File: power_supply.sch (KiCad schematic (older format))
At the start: 95 parts, among them J1 USB-IN, J2 USB OUT, Q1 SI4174DY, Q2 SI4463CDY, Q3 SI4463CDY, U1 LM3914, U10 FDC6392S, U11 MCP6041, U2 TPD2E001, U3 MIC2185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

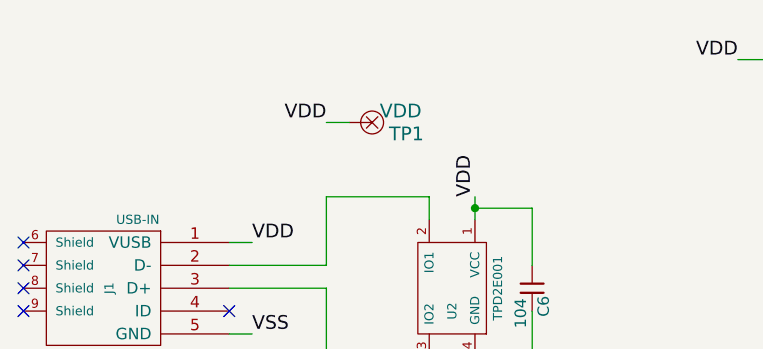
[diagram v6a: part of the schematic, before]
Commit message: Added test points
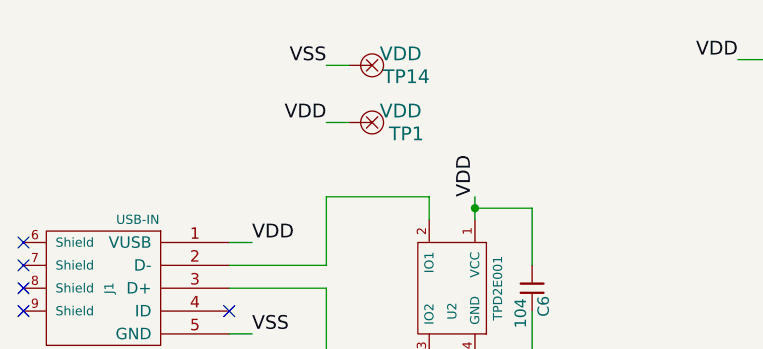
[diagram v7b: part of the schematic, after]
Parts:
- added TP14: VDD, TP, symbol TP
- TP1, TP10, TP11, TP12, TP13, TP2, TP3, TP4, TP6, TP7, TP8, TP9: footprint (none) -> TP; Product Number (none) -> 5000K-ND; Vendor (none) -> Digikey
- TP5: footprint (none) -> TP
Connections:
- net VSS: now also TP14.1
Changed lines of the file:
@@
 F 0 "TP1" H 2450 1050 60  0000 C CNN
 F 1 "VDD" H 2425 1150 60  0000 C CNN
-F 2 "" H 2300 1100 60  0000 C CNN
-F 3 "" H 2300 1100 60  0000 C CNN
+F 2 "TP" H 2300 1100 60  0001 C CNN
+F 3 "http://www.keyelco.com/userAssets/file/M60-2p60.pdf" H 2300 1100 60  0001 C CNN
+F 4 "5000K-ND" H 2300 1100 60  0001 C CNN "Product Number"
+F 5 "Digikey" H 2300 1100 60  0001 C CNN "Vendor"
 	1    2300 1100
 	1    0    0    -1
@@
 Text Label 2100 1100 2    60   ~ 0
 VDD
-$Comp
-L TP TP6
-U 1 1 53A9ABF0
-P 7600 1950
-F 0 "TP6" H 7750 1900 60  0000 C CNN
-F 1 "VBAT" H 7725 2000 60  0000 C CNN
-F 2 "" H 7600 1950 60  0000 C CNN
-F 3 "" H 7600 1950 60  0000 C CNN
-	1    7600 1950
-	1    0    0    -1
-$EndComp
 Wire Wire Line
 	4500 1975 4500 1625
@@
 	7500 1950 7375 1950
 Connection ~ 7375 1950
-$Comp
-L TP TP11
-U 1 1 53A9AEB5
-P 10200 1575
-F 0 "TP11" H 10350 1525 60  0000 C CNN
-F 1 "VSYS" H 10325 1625 60  0000 C CNN
-F 2 "" H 10200 1575 60  0000 C CNN
-F 3 "" H 10200 1575 60  0000 C CNN
-	1    10200 1575
-	1    0    0    -1
-$EndComp
 Wire Wire Line
 	10100 1575 9975 1575
 Connection ~ 9975 1575
-$Comp
-L TP TP10
-U 1 1 53A9B01C
-P 9800 3075
-F 0 "TP10" H 9950 3025 60  0000 C CNN
-F 1 "RS+" H 9925 3125 60  0000 C CNN
-F 2 "" H 9800 3075 60  0000 C CNN
-F 3 "" H 9800 3075 60  0000 C CNN
-	1    9800 3075
-	0    -1   -1   0
-$EndComp
 Wire Wire Line
 	9800 3175 9800 3250
 Connection ~ 9800 3250
-$Comp
-L TP TP9
-U 1 1 53A9B185
-P 9775 3875
-F 0 "TP9" H 9925 3825 60  0000 C CNN
-F 1 "RS-" H 9900 3925 60  0000 C CNN
-F 2 "" H 9775 3875 60  0000 C CNN
-F 3 "" H 9775 3875 60  0000 C CNN
-	1    9775 3875
-	0    1    1    0
-$EndComp
 Wire Wire Line
 	9775 3700 9775 3775
 Connection ~ 9775 3700
-$Comp
-L TP TP13
-U 1 1 53A9B5CD
-P 10625 4025
-F 0 "TP13" H 10775 3975 60  0000 C CNN
-F 1 "VDISP" H 10750 4075 60  0000 C CNN
-F 2 "" H 10625 4025 60  0000 C CNN
-F 3 "" H 10625 4025 60  0000 C CNN
-	1    10625 4025
-	0    -1   -1   0
-$EndComp
 Wire Wire Line
 	10625 4125 10625 4250
 Connection ~ 10625 4250
-$Comp
-L TP TP8
-U 1 1 53A9B73A
-P 9000 3850
-F 0 "TP8" H 9150 3800 60  0000 C CNN
-F 1 "VSENSE" H 9125 3900 60  0000 C CNN
-F 2 "" H 9000 3850 60  0000 C CNN
-F 3 "" H 9000 3850 60  0000 C CNN
-	1    9000 3850
-	0    1    1    0
-$EndComp
 Wire Wire Line
 	9000 3750 9000 3575
 Connection ~ 9000 3575
-$Comp
-L TP TP12
-U 1 1 53A9B8B3
-P 10375 4975
-F 0 "TP12" H 10525 4925 60  0000 C CNN
-F 1 "VSW_OUT" H 10500 5025 60  0000 C CNN
-F 2 "" H 10375 4975 60  0000 C CNN
-F 3 "" H 10375 4975 60  0000 C CNN
-	1    10375 4975
-	0    1    1    0
-$EndComp
 Connection ~ 10375 4800
-$Comp
-L TP TP2
-U 1 1 53A9BA2E
-P 4875 6650
-F 0 "TP2" H 5025 6600 60  0000 C CNN
-F 1 "VUSB" H 5000 6700 60  0000 C CNN
-F 2 "" H 4875 6650 60  0000 C CNN
-F 3 "" H 4875 6650 60  0000 C CNN
-	1    4875 6650
-	-1   0    0    1
-$EndComp
 Wire Wire Line
 	4975 6650 5075 6650
 Connection ~ 5075 6650
-$Comp
-L TP TP3
-U 1 1 53A9BBA0
-P 5900 6800
-F 0 "TP3" H 6050 6750 60  0000 C CNN
-F 1 "D-" H 6025 6850 60  0000 C CNN
-F 2 "" H 5900 6800 60  0000 C CNN
-F 3 "" H 5900 6800 60  0000 C CNN
-	1    5900 6800
-	0    1    1    0
-$EndComp
 Wire Wire Line
 	5900 6700 5900 6625
 Connection ~ 5900 6625
-$Comp
-L TP TP4
-U 1 1 53A9BD14
-P 6625 6775
-F 0 "TP4" H 6775 6725 60  0000 C CNN
-F 1 "D+" H 6750 6825 60  0000 C CNN
-F 2 "" H 6625 6775 60  0000 C CNN
-F 3 "" H 6625 6775 60  0000 C CNN
-	1    6625 6775
-	0    1    1    0
-$EndComp
 Wire Wire Line
 	6625 6675 6625 6625
 Connection ~ 6625 6625
-$Comp
-L TP TP7
-U 1 1 53A9C03D
-P 7725 4975
-F 0 "TP7" H 7875 4925 60  0000 C CNN
-F 1 "VSW_REF" H 7850 5025 60  0000 C CNN
-F 2 "" H 7725 4975 60  0000 C CNN
-F 3 "" H 7725 4975 60  0000 C CNN
-	1    7725 4975
-	-1   0    0    1
-$EndComp
 Connection ~ 7950 4975
 $Comp
@@
 F 0 "TP5" H 6975 3400 60  0000 C CNN
 F 1 "VREG" H 6950 3500 60  0000 C CNN
-F 2 "" H 6825 3450 60  0000 C CNN
+F 2 "TP" H 6825 3450 60  0001 C CNN
 F 3 "" H 6825 3450 60  0000 C CNN
 	1    6825 3450
@@
 Connection ~ 9350 850
 Connection ~ 9500 850
+Wire Wire Line
+	2200 850  2100 850
+Text Label 2100 850  2    60   ~ 0
+VSS
+$Comp
+L TP TP2
+U 1 1 53A9D1FA
+P 4875 6650
+F 0 "TP2" H 5025 6600 60  0000 C CNN
+F 1 "VUSB" H 5000 6700 60  0000 C CNN
+F 2 "TP" H 4875 6650 60  0001 C CNN
+F 3 "http://www.keyelco.com/userAssets/file/M60-2p60.pdf" H 4875 6650 60  0001 C CNN
+F 4 "5000K-ND" H 4875 6650 60  0001 C CNN "Product Number"
+F 5 "Digikey" H 4875 6650 60  0001 C CNN "Vendor"
+	1    4875 6650
+	-1   0    0    1
+$EndComp
+$Comp
+L TP TP3
+U 1 1 53A9D210
+P 5900 6800
+F 0 "TP3" H 6050 6750 60  0000 C CNN
+F 1 "D-" H 6025 6850 60  0000 C CNN
+F 2 "TP" H 5900 6800 60  0001 C CNN
+F 3 "http://www.keyelco.com/userAssets/file/M60-2p60.pdf" H 5900 6800 60  0001 C CNN
+F 4 "5000K-ND" H 5900 6800 60  0001 C CNN "Product Number"
+F 5 "Digikey" H 5900 6800 60  0001 C CNN "Vendor"
+	1    5900 6800
+	0    1    1    0
+$EndComp
+$Comp
+L TP TP4
+U 1 1 53A9D226
+P 6625 6775
+F 0 "TP4" H 6775 6725 60  0000 C CNN
+F 1 "D+" H 6750 6825 60  0000 C CNN
+F 2 "TP" H 6625 6775 60  0001 C CNN
+F 3 "http://www.keyelco.com/userAssets/file/M60-2p60.pdf" H 6625 6775 60  0001 C CNN
+F 4 "5000K-ND" H 6625 6775 60  0001 C CNN "Product Number"
+F 5 "Digikey" H 6625 6775 60  0001 C CNN "Vendor"
+	1    6625 6775
+	0    1    1    0
+$EndComp
+$Comp
+L TP TP7
+U 1 1 53A9D23C
+P 7725 4975
+F 0 "TP7" H 7875 4925 60  0000 C CNN
+F 1 "VSW_REF" H 7850 5025 60  0000 C CNN
+F 2 "TP" H 7725 4975 60  0001 C CNN
+F 3 "http://www.keyelco.com/userAssets/file/M60-2p60.pdf" H 7725 4975 60  0001 C CNN
+F 4 "5000K-ND" H 7725 4975 60  0001 C CNN "Product Number"
+F 5 "Digikey" H 7725 4975 60  0001 C CNN "Vendor"
+	1    7725 4975
+	-1   0    0    1
+$EndComp
+$Comp
+L TP TP12
+U 1 1 53A9D252
+P 10375 4975
+F 0 "TP12" H 10525 4925 60  0000 C CNN
+F 1 "VSW_OUT" H 10500 5025 60  0000 C CNN
+F 2 "TP" H 10375 4975 60  0001 C CNN
+F 3 "http://www.keyelco.com/userAssets/file/M60-2p60.pdf" H 10375 4975 60  0001 C CNN
+F 4 "5000K-ND" H 10375 4975 60  0001 C CNN "Product Number"
+F 5 "Digikey" H 10375 4975 60  0001 C CNN "Vendor"
+	1    10375 4975
+	0    1    1    0
+$EndComp
+$Comp
+L TP TP13
+U 1 1 53A9D25A
+P 10625 4025
+F 0 "TP13" H 10775 3975 60  0000 C CNN
+F 1 "VDISP" H 10750 4075 60  0000 C CNN
+F 2 "TP" H 10625 4025 60  0001 C CNN
+F 3 "http://www.keyelco.com/userAssets/file/M60-2p60.pdf" H 10625 4025 60  0001 C CNN
+F 4 "5000K-ND" H 10625 4025 60  0001 C CNN "Product Number"
+F 5 "Digikey" H 10625 4025 60  0001 C CNN "Vendor"
+	1    10625 4025
+	0    -1   -1   0
+$EndComp
+$Comp
+L TP TP9
+U 1 1 53A9D270
+P 9775 3875
+F 0 "TP9" H 9925 3825 60  0000 C CNN
+F 1 "RS-" H 9900 3925 60  0000 C CNN
+F 2 "TP" H 9775 3875 60  0001 C CNN
+F 3 "http://www.keyelco.com/userAssets/file/M60-2p60.pdf" H 9775 3875 60  0001 C CNN
+F 4 "5000K-ND" H 9775 3875 60  0001 C CNN "Product Number"
+F 5 "Digikey" H 9775 3875 60  0001 C CNN "Vendor"
+	1    9775 3875
+	0    1    1    0
+$EndComp
+$Comp
+L TP TP8
+U 1 1 53A9D278
+P 9000 3850
+F 0 "TP8" H 9150 3800 60  0000 C CNN
+F 1 "VSENSE" H 9125 3900 60  0000 C CNN
+F 2 "TP" H 9000 3850 60  0001 C CNN
+F 3 "http://www.keyelco.com/userAssets/file/M60-2p60.pdf" H 9000 3850 60  0001 C CNN
+F 4 "5000K-ND" H 9000 3850 60  0001 C CNN "Product Number"
+F 5 "Digikey" H 9000 3850 60  0001 C CNN "Vendor"
+	1    9000 3850
+	0    1    1    0
+$EndComp
+$Comp
+L TP TP6
+U 1 1 53A9D28E
+P 7600 1950
+F 0 "TP6" H 7750 1900 60  0000 C CNN
+F 1 "VBAT" H 7725 2000 60  0000 C CNN
+F 2 "TP" H 7600 1950 60  0001 C CNN
+F 3 "http://www.keyelco.com/userAssets/file/M60-2p60.pdf" H 7600 1950 60  0001 C CNN
+F 4 "5000K-ND" H 7600 1950 60  0001 C CNN "Product Number"
+F 5 "Digikey" H 7600 1950 60  0001 C CNN "Vendor"
+	1    7600 1950
+	1    0    0    -1
+$EndComp
+$Comp
+L TP TP11
+U 1 1 53A9D2C0
+P 10200 1575
+F 0 "TP11" H 10350 1525 60  0000 C CNN
+F 1 "VSYS" H 10325 1625 60  0000 C CNN
+F 2 "TP" H 10200 1575 60  0001 C CNN
+F 3 "http://www.keyelco.com/userAssets/file/M60-2p60.pdf" H 10200 1575 60  0001 C CNN
+F 4 "5000K-ND" H 10200 1575 60  0001 C CNN "Product Number"
+F 5 "Digikey" H 10200 1575 60  0001 C CNN "Vendor"
+	1    10200 1575
+	1    0    0    -1
+$EndComp
+$Comp
+L TP TP10
+U 1 1 53A9D48F
+P 9800 3075
+F 0 "TP10" H 9950 3025 60  0000 C CNN
+F 1 "RS+" H 9925 3125 60  0000 C CNN
+F 2 "TP" H 9800 3075 60  0001 C CNN
+F 3 "http://www.keyelco.com/userAssets/file/M60-2p60.pdf" H 9800 3075 60  0001 C CNN
+F 4 "5000K-ND" H 9800 3075 60  0001 C CNN "Product Number"
+F 5 "Digikey" H 9800 3075 60  0001 C CNN "Vendor"
+	1    9800 3075
+	0    -1   -1   0
+$EndComp
+$Comp
+L TP TP14
+U 1 1 53A9D69D
+P 2300 850
+F 0 "TP14" H 2450 800 60  0000 C CNN
+F 1 "VDD" H 2425 900 60  0000 C CNN
+F 2 "TP" H 2300 850 60  0001 C CNN
+F 3 "http://www.keyelco.com/userAssets/file/M60-2p60.pdf" H 2300 850 60  0001 C CNN
+F 4 "5000K-ND" H 2300 850 60  0001 C CNN "Product Number"
+F 5 "Digikey" H 2300 850 60  0001 C CNN "Vendor"
+	1    2300 850
+	1    0    0    -1
+$EndComp
 $EndSCHEMATC

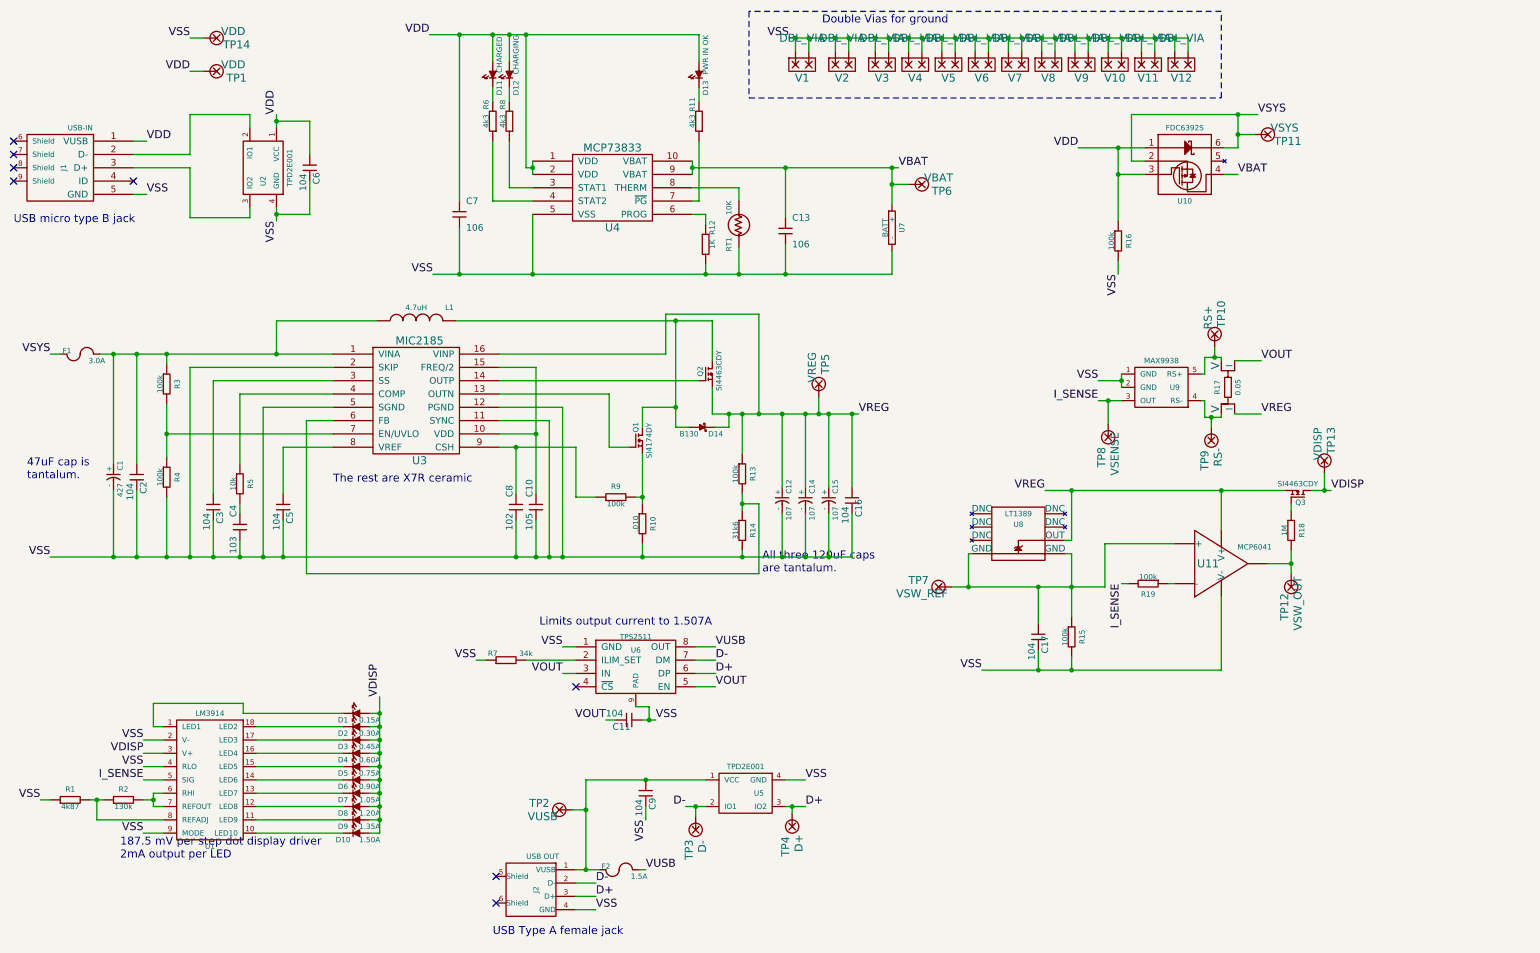
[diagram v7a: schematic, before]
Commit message: Added silkscreen
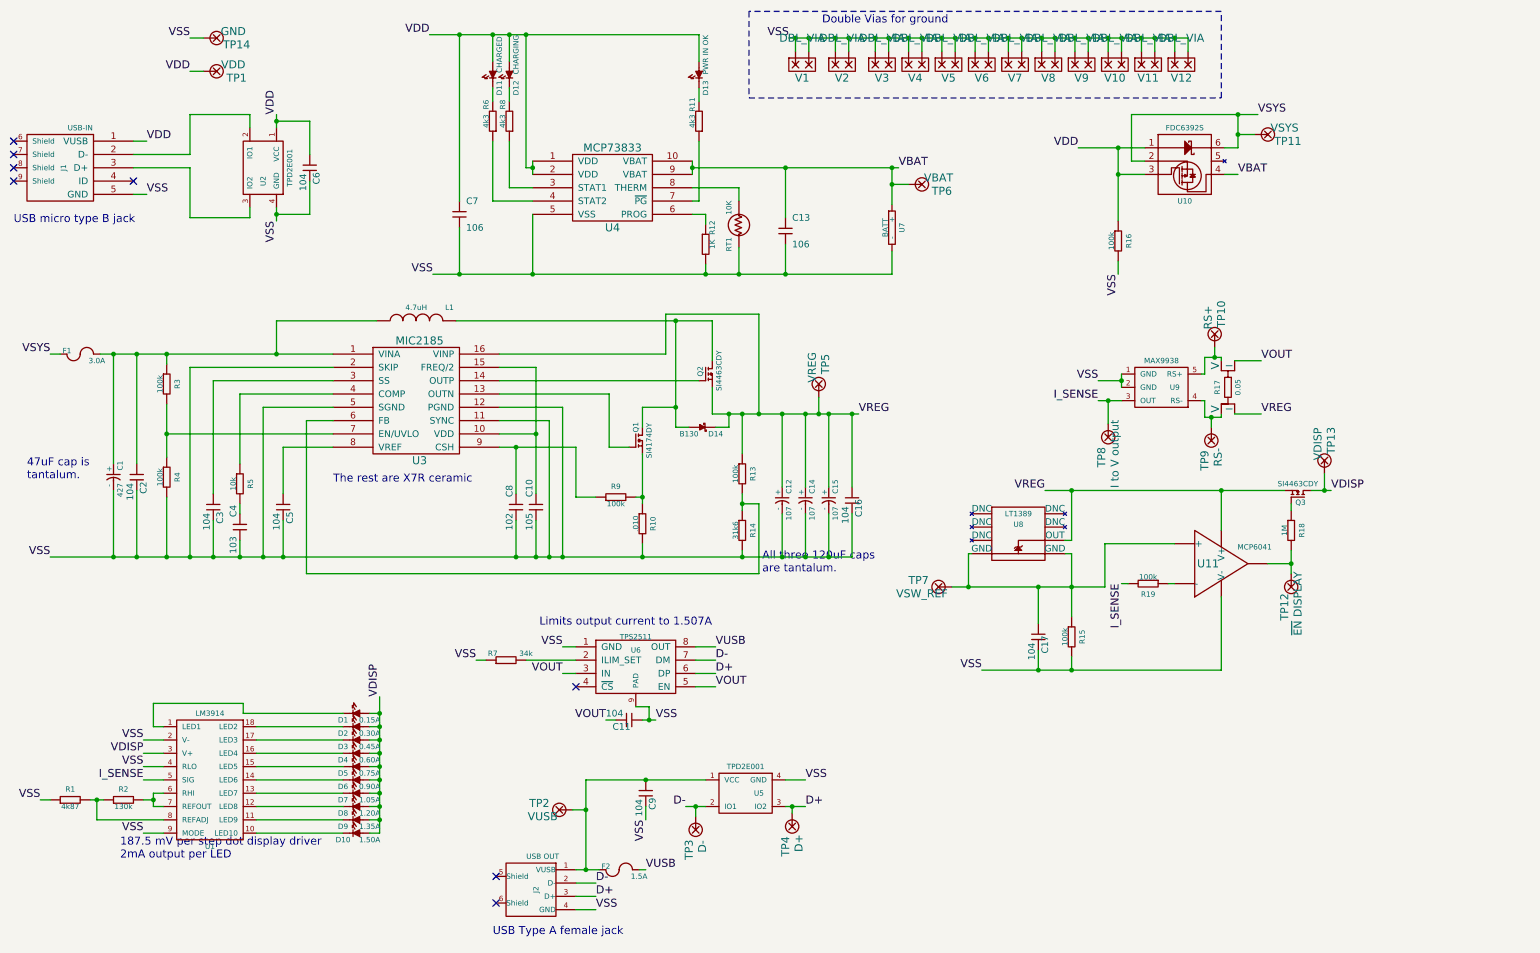
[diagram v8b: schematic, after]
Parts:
- TP12: value VSW_OUT -> ~EN DISPLAY
- TP14: value VDD -> GND
- TP8: value VSENSE -> I to V output
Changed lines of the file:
@@
 Sheet 1 1
 Title "USB Power Pack"
-Date "24 jun 2014"
+Date "25 jun 2014"
 Rev "2"
 Comp "AMP Lab"
@@
 P 10375 4975
 F 0 "TP12" H 10525 4925 60  0000 C CNN
-F 1 "VSW_OUT" H 10500 5025 60  0000 C CNN
+F 1 "~EN DISPLAY" H 10500 5025 60  0000 C CNN
 F 2 "TP" H 10375 4975 60  0001 C CNN
 F 3 "http://www.keyelco.com/userAssets/file/M60-2p60.pdf" H 10375 4975 60  0001 C CNN
@@
 P 9000 3850
 F 0 "TP8" H 9150 3800 60  0000 C CNN
-F 1 "VSENSE" H 9125 3900 60  0000 C CNN
+F 1 "I to V output" H 9125 3900 60  0000 C CNN
 F 2 "TP" H 9000 3850 60  0001 C CNN
 F 3 "http://www.keyelco.com/userAssets/file/M60-2p60.pdf" H 9000 3850 60  0001 C CNN
@@
 P 2300 850
 F 0 "TP14" H 2450 800 60  0000 C CNN
-F 1 "VDD" H 2425 900 60  0000 C CNN
+F 1 "GND" H 2425 900 60  0000 C CNN
 F 2 "TP" H 2300 850 60  0001 C CNN
 F 3 "http://www.keyelco.com/userAssets/file/M60-2p60.pdf" H 2300 850 60  0001 C CNN
